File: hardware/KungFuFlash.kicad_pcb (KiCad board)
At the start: 2 copper layers, 60.6 x 62 mm, 40 parts, among them J1 USB Power, J2 USB_B_Micro, J4 SWD, Q1 BC817, SW1 Reset, SW2 Menu, SW3 Special, U1 C64-Exp-Port, U2 AMS1117-3.3, U3 STM32F405RGTx, Y1 8MHz

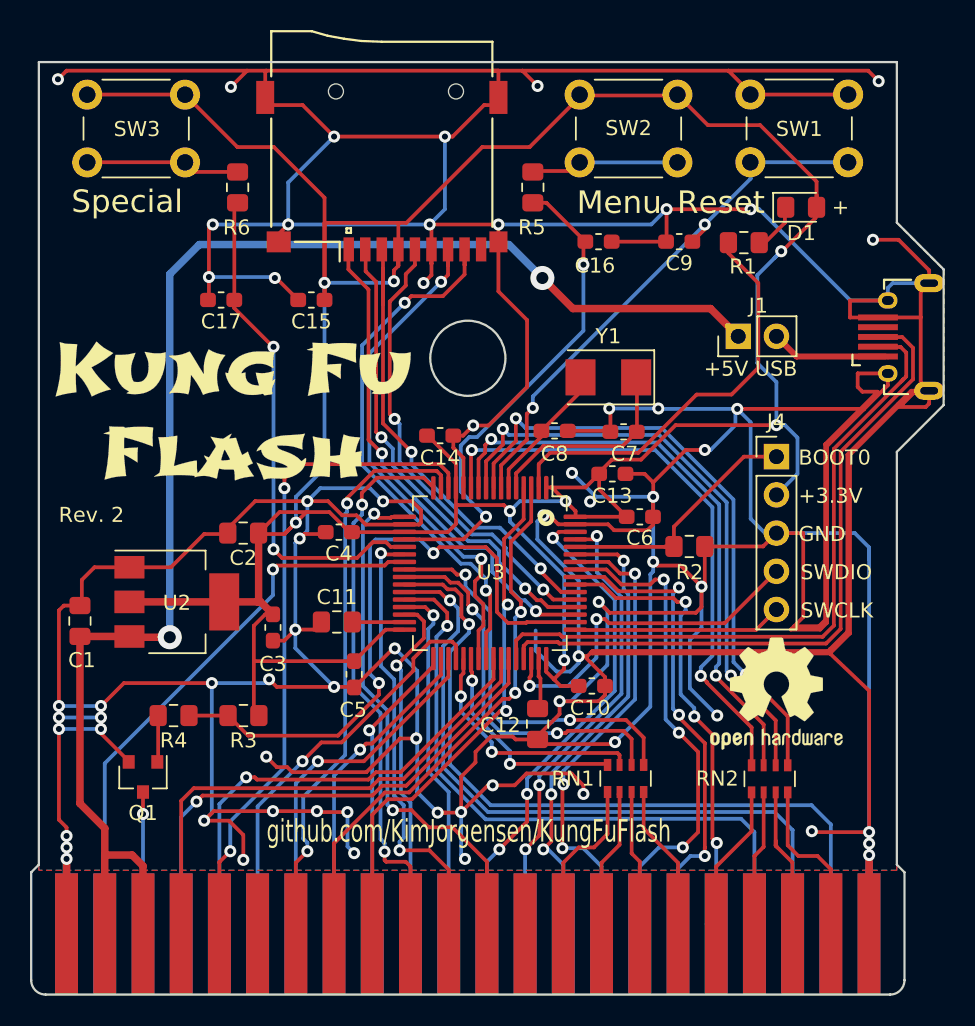
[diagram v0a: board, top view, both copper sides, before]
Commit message: Change to LQFP-100, replace resitor network, add DMA
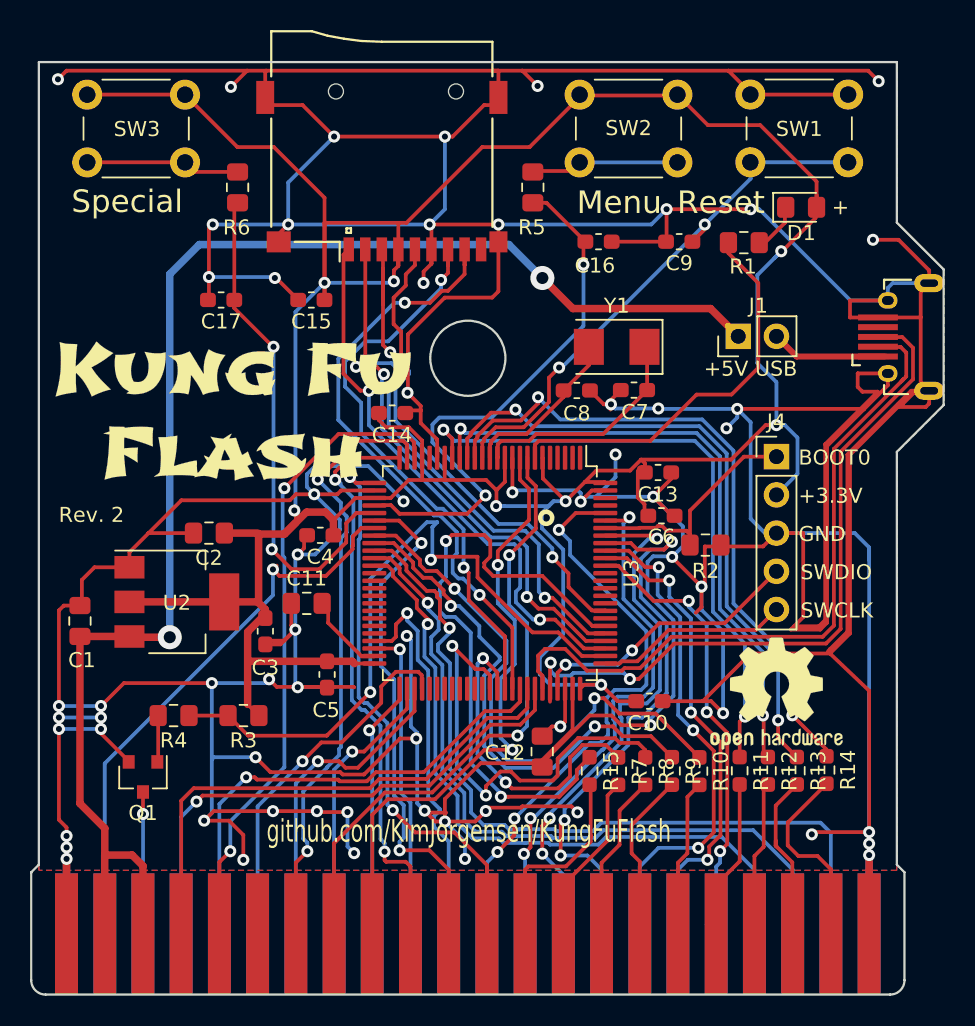
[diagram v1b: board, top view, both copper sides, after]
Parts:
- removed RN1, RN2: 100R, Resistor_SMD:R_Array_Convex_4x0603
- added R10: 100R, Resistor_SMD:R_0603_1608Metric_Pad0.98x0.95mm_HandSolder, F.Cu at (120.3, 115.3)
- added R11: 100R, Resistor_SMD:R_0603_1608Metric_Pad0.98x0.95mm_HandSolder, F.Cu at (123.0, 115.3)
- added R12: 100R, Resistor_SMD:R_0603_1608Metric_Pad0.98x0.95mm_HandSolder, F.Cu at (124.8, 115.3)
- added R13: 100R, Resistor_SMD:R_0603_1608Metric_Pad0.98x0.95mm_HandSolder, F.Cu at (126.8, 115.3)
- added R14: 100R, Resistor_SMD:R_0603_1608Metric_Pad0.98x0.95mm_HandSolder, F.Cu at (128.7, 115.3)
- added R15: 100R, Resistor_SMD:R_0603_1608Metric_Pad0.98x0.95mm_HandSolder, F.Cu at (113.0, 115.3)
- added R7: 100R, Resistor_SMD:R_0603_1608Metric_Pad0.98x0.95mm_HandSolder, F.Cu at (114.9, 115.3)
- added R8: 100R, Resistor_SMD:R_0603_1608Metric_Pad0.98x0.95mm_HandSolder, F.Cu at (116.7, 115.3)
- added R9: 100R, Resistor_SMD:R_0603_1608Metric_Pad0.98x0.95mm_HandSolder, F.Cu at (118.5, 115.3)
- U3: value STM32F405RGTx -> STM32F407VETx; footprint Package_QFP:LQFP-64_10x10mm_P0.5mm -> Package_QFP:LQFP-100_14x14mm_P0.5mm
- moved C10 3.96 mm to (117.0, 110.7)
- moved C14 3.53 mm to (99.9, 91.5)
- moved C8 3.06 mm to (112.1, 90.0)
- moved C13 3.04 mm to (117.5, 95.5)
- moved C7 2.86 mm to (115.9, 90.0)
- moved C11 2.35 mm to (94.2, 104.2)
- moved C2 2.28 mm to (87.7, 99.5)
- moved Y1 2.10 mm to (114.8, 87.1)
- moved C12 1.86 mm to (109.8, 114.0)
- moved C5 1.80 mm to (95.5, 108.9)
- moved C6 1.44 mm to (117.8, 98.4)
- moved C4 1.25 mm to (95.1, 99.7)
- moved R2 1.07 mm to (120.7, 100.3)
- moved C3 0.56 mm to (91.4, 106.0)
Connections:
- U1 pad 13: Net-(U1-Pad13) -> /CDMA
- U3 pad 1: +3V3 -> Net-(U3-Pad1)
- U3 pad 10: /D2 -> GND
- U3 pad 11: /D3 -> +3V3
- U3 pad 12: GND -> Net-(C7-Pad2)
- U3 pad 13: +3V3 -> Net-(C8-Pad1)
- U3 pad 14: /R~W -> /~RST
- U3 pad 15: /~IO1 -> /D0
- U3 pad 16: /~IO2 -> /D1
- U3 pad 17: /BA -> /D2
- U3 pad 18: GND -> /D3
- U3 pad 2: /~LED -> Net-(U3-Pad2)
- U3 pad 20: /MENU -> GND
- U3 pad 21: /SPECIAL -> Net-(U3-Pad21)
- U3 pad 22: /~ROML -> +3V3
- U3 pad 23: /~ROMH -> /R~W
- U3 pad 24: /D4 -> /~IO1
- U3 pad 25: /D5 -> /~IO2
- U3 pad 26: /A0 -> /BA
- U3 pad 27: /A1 -> GND
- U3 pad 28: /A2 -> +3V3
- U3 pad 29: /A10 -> /MENU
- U3 pad 3: /~GAME -> Net-(U3-Pad3)
- U3 pad 30: /A11 -> /SPECIAL
- U3 pad 31: Net-(C11-Pad2) -> /~ROML
- U3 pad 32: +3V3 -> /~ROMH
- U3 pad 33: /A12 -> /D4
- U3 pad 34: /A13 -> /D5
- U3 pad 35: /A14 -> /A0
- U3 pad 36: /A15 -> /A1
- U3 pad 37: /D6 -> /A2
- U3 pad 38: /D7 -> Net-(U3-Pad38)
- U3 pad 39: /SD_D0 -> Net-(U3-Pad39)
- U3 pad 4: /~EXROM -> Net-(U3-Pad4)
- U3 pad 40: /SD_D1 -> Net-(U3-Pad40)
- U3 pad 41: /PHI2 -> Net-(U3-Pad41)
- U3 pad 42: /~IRQ -> Net-(U3-Pad42)
- U3 pad 43: /~NMI -> Net-(U3-Pad43)
- U3 pad 44: /USB_DM -> Net-(U3-Pad44)
- U3 pad 45: /USB_DP -> Net-(U3-Pad45)
- U3 pad 46: /SWDIO -> Net-(U3-Pad46)
- U3 pad 47: Net-(C12-Pad1) -> /A10
- U3 pad 48: +3V3 -> /A11
- U3 pad 49: /SWCLK -> Net-(C11-Pad2)
- U3 pad 5: Net-(C7-Pad2) -> Net-(U3-Pad5)
- U3 pad 50: /~RST_O -> +3V3
- U3 pad 51: /SD_D2 -> /A12
- U3 pad 52: /SD_D3 -> /A13
- U3 pad 53: /SD_CK -> /A14
- U3 pad 54: /SD_CMD -> /A15
- U3 pad 55: /A3 -> Net-(U3-Pad55)
- U3 pad 56: /A4 -> Net-(U3-Pad56)
- U3 pad 57: /A5 -> Net-(U3-Pad57)
- U3 pad 58: /A6 -> Net-(U3-Pad58)
- U3 pad 59: /A7 -> Net-(U3-Pad59)
- U3 pad 6: Net-(C8-Pad1) -> +3V3
- U3 pad 60: /BOOT0 -> Net-(U3-Pad60)
- U3 pad 61: /A8 -> Net-(U3-Pad61)
- U3 pad 62: /A9 -> Net-(U3-Pad62)
- U3 pad 63: GND -> /D6
- U3 pad 64: +3V3 -> /D7
- U3 pad 7: /~RST -> /~LED
- U3 pad 8: /D0 -> /~GAME
- U3 pad 9: /D1 -> /~EXROM
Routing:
- net GND: track 751.1 -> 701.6 mm, vias 66 -> 63
- net /DMA: track 0.00 -> 41.4 mm, vias 0 -> 2
- net /D6: track 16.3 -> 29.7 mm
- net /CDMA: track 0.00 -> 13.3 mm
- net /SD_CK: track 30.7 -> 42.2 mm
- net /D4: track 26.9 -> 37.3 mm
- net /D5: track 25.6 -> 33.8 mm
- net +3V3: track 232.6 -> 239.6 mm
- net /D7: track 14.6 -> 21.5 mm
- net /A6: track 32.1 -> 38.6 mm
- net /A9: track 33.2 -> 38.7 mm
- net /~EXROM: track 35.3 -> 40.7 mm
- net /A7: track 31.4 -> 36.4 mm
- net /SWDIO: track 23.1 -> 18.4 mm
- net /~GAME: track 36.8 -> 41.3 mm
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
